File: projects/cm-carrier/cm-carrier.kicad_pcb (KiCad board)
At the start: 4 copper layers, 130 x 90 mm, 93 parts, among them J1 XA_5V_IN, J2 DEBUG_UART, J3 USB_C_HOST (USB2.0), J4 XA_USB1, J5 XA_USB2, J6 EC25-J Mini PCIe, J7 nanoSIM, J8 micro HDMI (Type D), J9 microSD, Q1 2N7002, Q2 2N7002, SW1 PWR_BUT, U1 TPS62132, U10 TPD4EUSB30, U11 TPD4EUSB30, U12 MagJack A70-112-331N126, U13 TPD4EUSB30, U14 TPD4EUSB30, U15 TPD4EUSB30, U16 RT9742SNGV, U17 RT9742GGJ5, U2 USB2514B-I/M2, U3 TPS2051CDBV, U4 TPS2051CDBV, U5 TPS2051CDBV, U6 USBLC6-2SC6, U7 USBLC6-2SC6, U8 USBLC6-2SC6, U9 TPD4E05U06DQA, Y1 24MHz CL=18pF

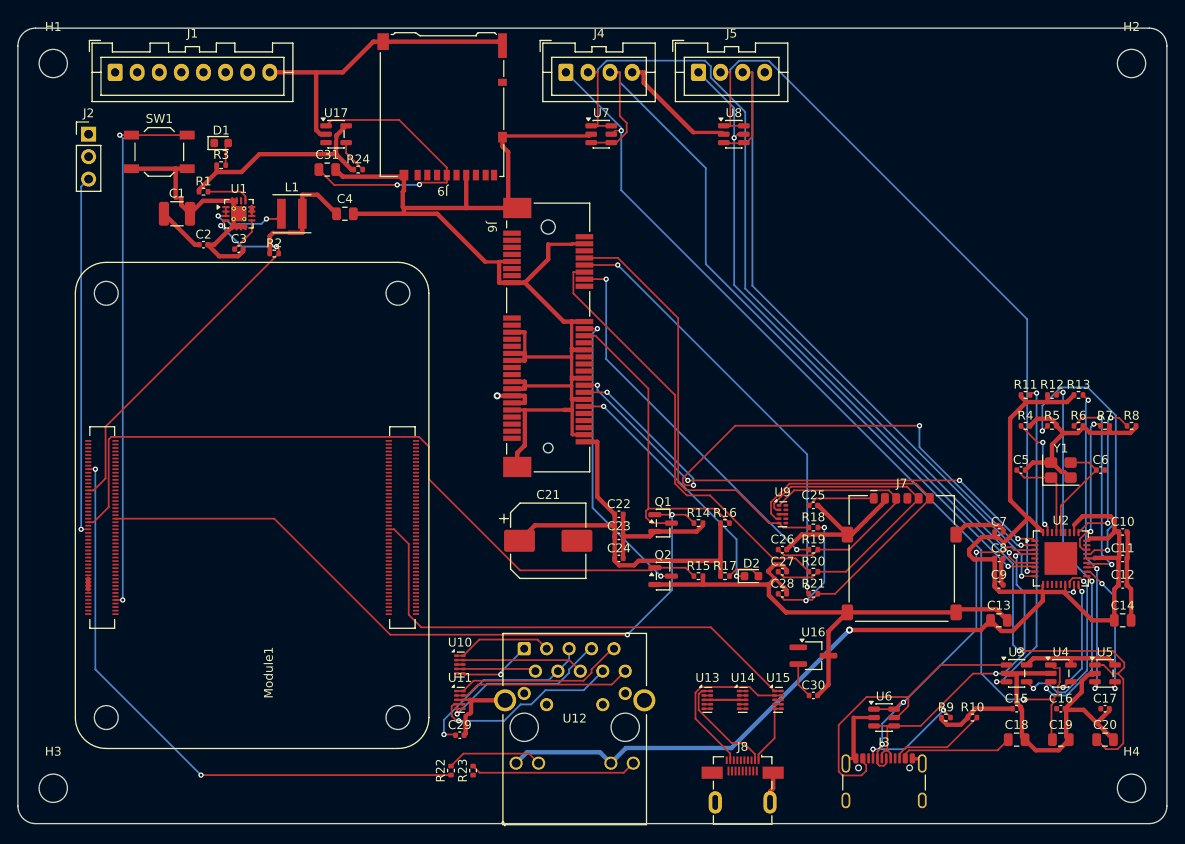
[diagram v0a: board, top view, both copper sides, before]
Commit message: cm-carrier: back to unrouted 4-layer board; Default netclass 0.127/0.1 for signal-only routing
Co-Authored-By: Claude Opus 5.5 <noreply@anthropic.com>
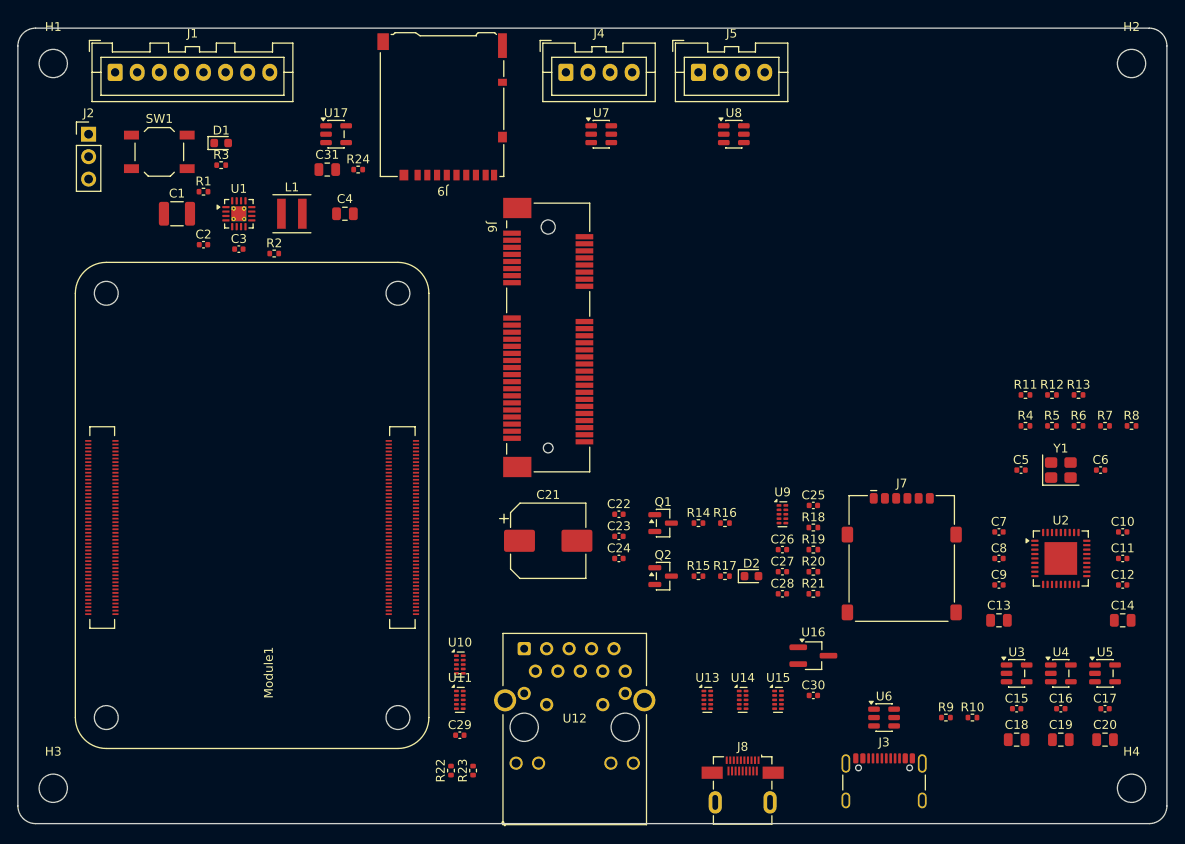
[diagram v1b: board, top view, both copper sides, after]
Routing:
- net GND: track 435.5 -> 0.00 mm
- net +3V3: track 177.8 -> 0.00 mm, vias 1 -> 0
- net /USB Hub/P4_VBUS: track 110.6 -> 0.00 mm, vias 2 -> 0
- net /USB Hub/P3_VBUS: track 108.0 -> 0.00 mm, vias 2 -> 0
- net /USB Hub/P3_DM: track 97.0 -> 0.00 mm, vias 1 -> 0
- net /USB Hub/P3_DP: track 91.0 -> 0.00 mm, vias 1 -> 0
- net /USB Hub/P4_DM: track 86.4 -> 0.00 mm, vias 1 -> 0
- net LTE_AIRPLANE: track 85.9 -> 0.00 mm
- net /USB Hub/P4_DP: track 84.2 -> 0.00 mm, vias 1 -> 0
- net LTE_RESET: track 83.9 -> 0.00 mm, vias 2 -> 0
- net ETH_LED2_N: track 68.6 -> 0.00 mm, vias 2 -> 0
- net LTE_USB_P: track 68.3 -> 0.00 mm, vias 4 -> 0
- net +3V3_LTE: track 65.9 -> 0.00 mm, vias 1 -> 0
- net /CM/PWR_BUT: track 61.2 -> 0.00 mm, vias 2 -> 0
- net LTE_USB_N: track 58.6 -> 0.00 mm, vias 4 -> 0
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
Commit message: cm-carrier: 4-layer Freerouting trial imported via import_specctra_ses_native (138 unconnected, mostly plane nets)
Co-Authored-By: Claude Opus 5.5 <noreply@anthropic.com>
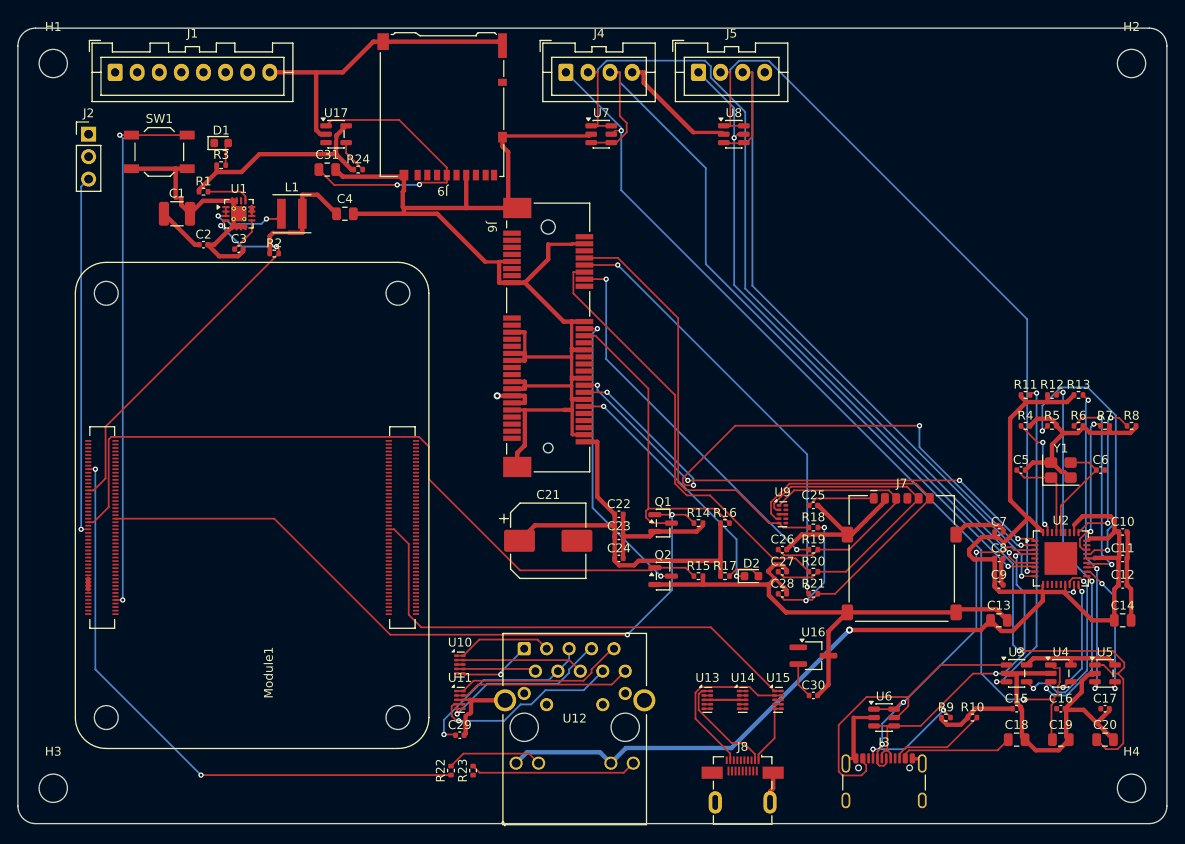
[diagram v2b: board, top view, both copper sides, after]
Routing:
- net GND: track 0.00 -> 435.5 mm
- net +3V3: track 0.00 -> 177.8 mm, vias 0 -> 1
- net /USB Hub/P4_VBUS: track 0.00 -> 110.6 mm, vias 0 -> 2
- net /USB Hub/P3_VBUS: track 0.00 -> 108.0 mm, vias 0 -> 2
- net /USB Hub/P3_DM: track 0.00 -> 97.0 mm, vias 0 -> 1
- net /USB Hub/P3_DP: track 0.00 -> 91.0 mm, vias 0 -> 1
- net /USB Hub/P4_DM: track 0.00 -> 86.4 mm, vias 0 -> 1
- net LTE_AIRPLANE: track 0.00 -> 85.9 mm
- net /USB Hub/P4_DP: track 0.00 -> 84.2 mm, vias 0 -> 1
- net LTE_RESET: track 0.00 -> 83.9 mm, vias 0 -> 2
- net ETH_LED2_N: track 0.00 -> 68.6 mm, vias 0 -> 2
- net LTE_USB_P: track 0.00 -> 68.3 mm, vias 0 -> 4
- net +3V3_LTE: track 0.00 -> 65.9 mm, vias 0 -> 1
- net /CM/PWR_BUT: track 0.00 -> 61.2 mm, vias 0 -> 2
- net LTE_USB_N: track 0.00 -> 58.6 mm, vias 0 -> 4
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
